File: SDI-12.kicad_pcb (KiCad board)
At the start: 2 copper layers, 61 x 30.3 mm, 44 parts, among them J1 USB_B_Micro, J2 Conn_SWD, J3 SDI-12_OUT, J4 SDI12_POWER, Q1 BSS138, Q2 BSS138, Q3 BSS138, U1 LDI1117-3.3H, U2 STM32F103C8Tx, U3 74LVC1G125GW,125, Y1 24MHz 15pF

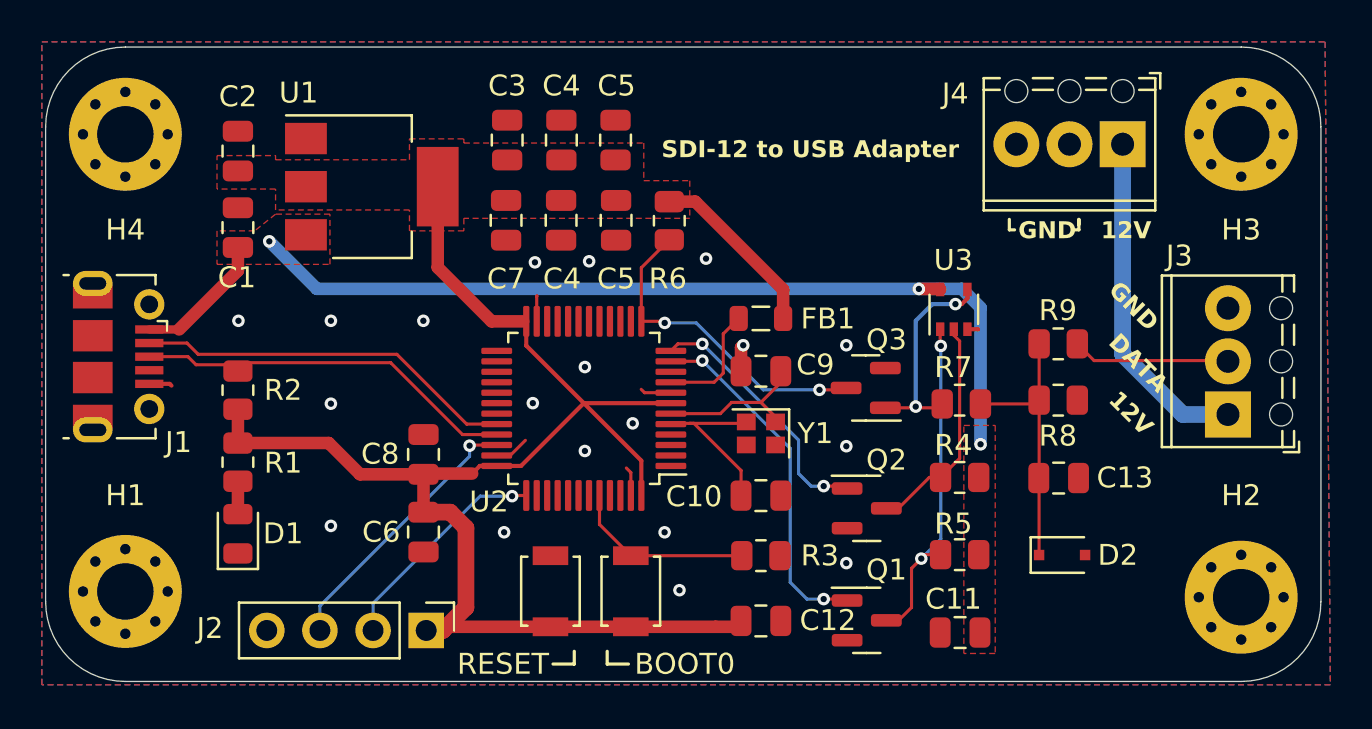
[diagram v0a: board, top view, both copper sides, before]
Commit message: - Crystal oscillator value changed to proper 16MHz - Minor font changes - Readme document - git lfs for readme graphics
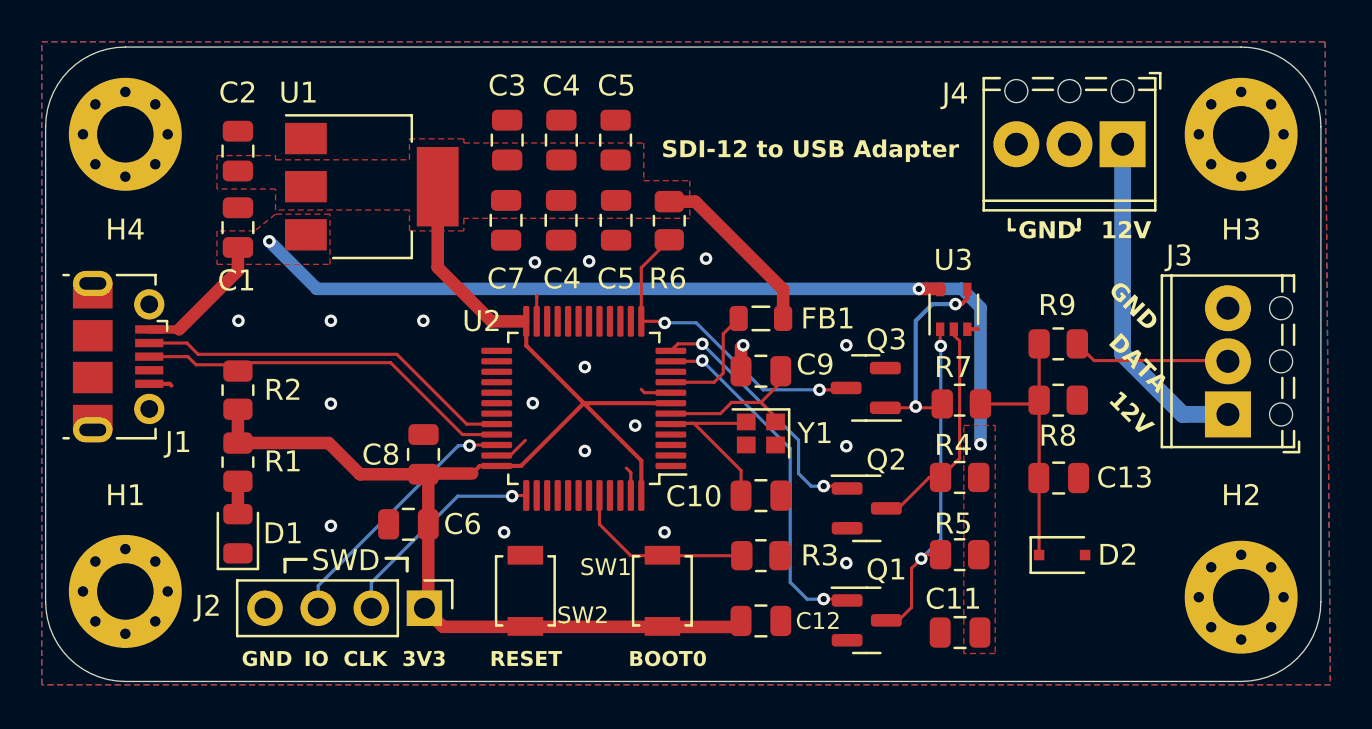
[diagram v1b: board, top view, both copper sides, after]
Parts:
- removed BOOT0: SW_Push, Button_Switch_SMD:SW_SPST_B3U-1000P
- removed RESET: RESET_SW, Button_Switch_SMD:SW_SPST_B3U-1000P
- added SW1: SW_Push, Button_Switch_SMD:SW_SPST_B3U-1000P, F.Cu at (66.5, 42.8)
- added SW2: RESET_SW, Button_Switch_SMD:SW_SPST_B3U-1000P, F.Cu at (59.9, 42.8)
- C10, C9: value 24pF -> 12pF
- Y1: value 24MHz 15pF -> 16MHz
- moved J2 1.06 mm to (55.1, 43.6)
- moved C6 0.81 mm to (54.3, 39.6), turned to 0 degrees
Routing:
- net 3V3: track 77.8 -> 75.2 mm
- net SWDIO: track 13.1 -> 12.4 mm
- net GND: vias 19 -> 18
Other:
- board text added: "3V3"
- board text added: "BOOT0"
- board text added: "CLK"
- board text added: "IO"
- board text added: "RESET"
- board text added: "SWD"

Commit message: - STM32F103 replaced with G431 counterpart - TXS0102x for voltage level shifting - Added LED's for I/O status
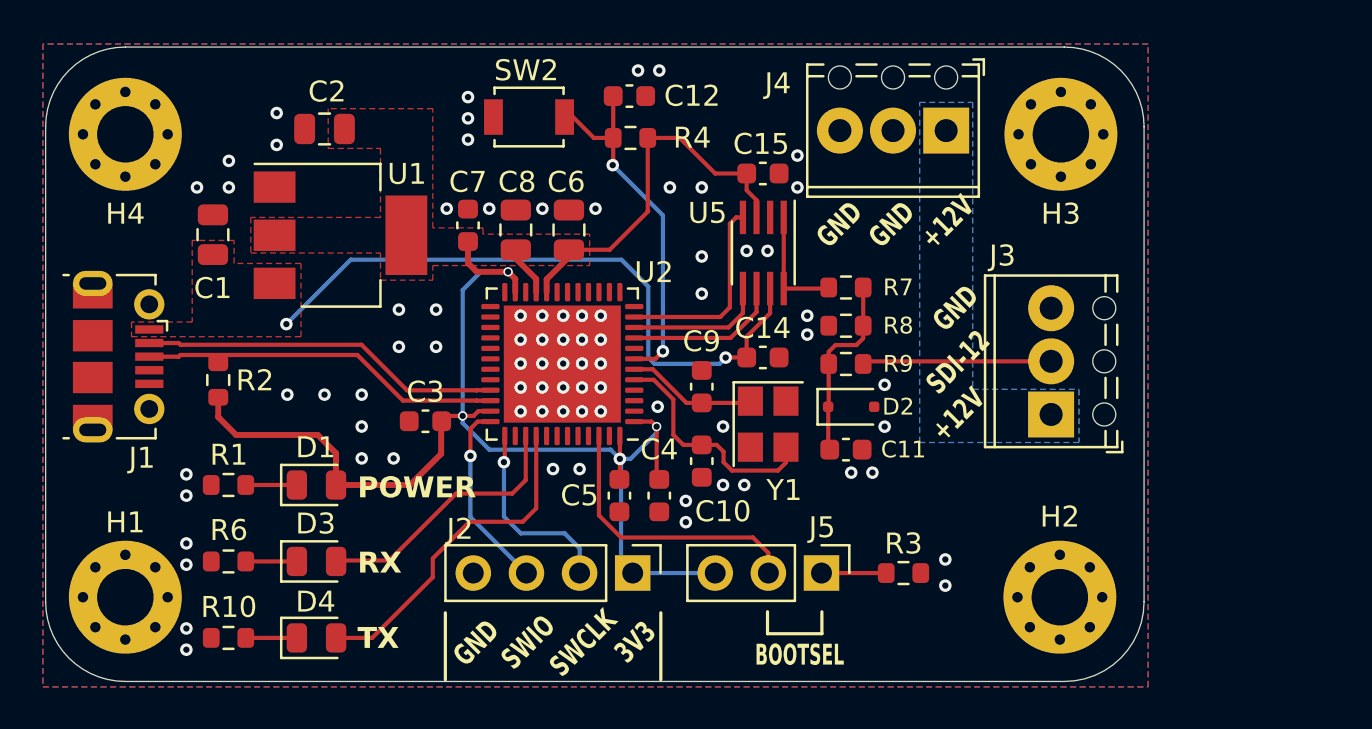
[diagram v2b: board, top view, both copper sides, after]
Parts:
- removed C13: 22nF, Capacitor_SMD:C_0805_2012Metric
- removed the C4 at (61.6, 21.2)
- removed the C4 at (61.6, 25.0)
- removed the C5 at (64.2, 21.2)
- removed the C5 at (64.3, 25.0)
- removed FB1: 100MHz 1kΩ, Inductor_SMD:L_0805_2012Metric
- removed Q1, Q2, Q3: BSS138, Package_TO_SOT_SMD:SOT-23
- removed R5: 2.2kΩ, Resistor_SMD:R_0805_2012Metric
- removed SW1: SW_Push, Button_Switch_SMD:SW_SPST_B3U-1000P
- removed U3: 74LVC1G125GW,125, Package_TO_SOT_SMD:SOT-353_SC-70-5
- added C14: 100nF, Capacitor_SMD:C_0603_1608Metric, F.Cu at (71.3, 31.6)
- added C15: 100nF, Capacitor_SMD:C_0603_1608Metric, F.Cu at (71.3, 22.8)
- added C4: 100nF, Capacitor_SMD:C_0603_1608Metric, F.Cu at (66.3, 38.2)
- added C5: 100nF, Capacitor_SMD:C_0603_1608Metric, F.Cu at (64.4, 38.2)
- added D3: USER_LED, LED_SMD:LED_0805_2012Metric, F.Cu at (49.9, 41.3)
- added D4: USER_LED_2, LED_SMD:LED_0805_2012Metric, F.Cu at (49.9, 45.0)
- added J5: BOOTSEL, Connector_PinHeader_2.54mm:PinHeader_1x03_P2.54mm_Vertical, F.Cu at (74.1, 41.9)
- added R10: xkΩ, Resistor_SMD:R_0603_1608Metric, F.Cu at (45.7, 45.0)
- added U5: TXS0102DCT, Package_SO:SSOP-8_2.95x2.8mm_P0.65mm, F.Cu at (71.3, 26.6)
- C10, C12, C3, C7, C9: footprint Capacitor_SMD:C_0805_2012Metric -> Capacitor_SMD:C_0603_1608Metric
- C11: value 100nF -> 22nF; footprint Capacitor_SMD:C_0805_2012Metric -> Capacitor_SMD:C_0603_1608Metric
- D1: value G_LED -> RED_LED
- R1: value 1kΩ -> xkΩ; footprint Resistor_SMD:R_0805_2012Metric -> Resistor_SMD:R_0603_1608Metric
- R2, R3, R7, R8, R9: footprint Resistor_SMD:R_0805_2012Metric -> Resistor_SMD:R_0603_1608Metric
- R4: value 2.2kΩ -> DNP; footprint Resistor_SMD:R_0805_2012Metric -> Resistor_SMD:R_0603_1608Metric
- R6: value 2.2kΩ -> xkΩ; footprint Resistor_SMD:R_0805_2012Metric -> Resistor_SMD:R_0603_1608Metric
- SW2: value RESET_SW -> RESET
- U2: value STM32F103C8Tx -> STM32G431CBUx; footprint Package_QFP:LQFP-48_7x7mm_P0.5mm -> Package_DFN_QFN:QFN-48-1EP_7x7mm_P0.5mm_EP5.6x5.6mm
- Y1: value 16MHz -> 24MHz; footprint Crystal:Crystal_SMD_2016-4Pin_2.0x1.6mm -> Crystal:Crystal_SMD_3225-4Pin_3.2x2.5mm
- moved R6 26.6 mm to (45.7, 41.3), turned to 0 degrees
- moved C12 25.9 mm to (64.9, 19.1)
- moved SW2 22.7 mm to (60.1, 20.1), turned to 180 degrees
- moved R4 22.6 mm to (65.0, 21.1)
- moved C6 16.0 mm to (62.0, 25.5), turned to -90 degrees
- moved C3 14.0 mm to (55.1, 34.6), turned to 0 degrees
- moved D2 12.3 mm to (75.5, 34.0)
- moved C8 11.6 mm to (59.5, 25.5)
- moved R8 10.8 mm to (75.2, 30.1), turned to 180 degrees
- moved C11 10.3 mm to (75.2, 36.0), turned to 0 degrees
- moved R9 10.2 mm to (75.2, 31.9)
- moved J2 10.1 mm to (65.1, 41.9)
- moved H2 8.67 mm to (85.5, 43.1)
- moved H3 8.62 mm to (85.5, 20.9)
- moved J4 8.46 mm to (80.0, 20.8)
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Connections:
- net SDI-12_DATA renamed SDI-12_BUS
- C11 pad 1: 5V -> Net-(D2-K)
- C12 pad 1: 3V3 -> NRST
- D1 pad 1: GND -> Net-(D1-K)
- D1 pad 2: Net-(D1-A) -> 3V3
- R1 pad 1: Net-(D1-A) -> GND
- R1 pad 2: 3V3 -> Net-(D1-K)
- R3 pad 1: BOOT0 -> Net-(J5-Pin_1)
- R4 pad 1: 5V -> 3V3
- R4 pad 2: Net-(Q2-D) -> NRST
- R6 pad 1: 3V3 -> GND
- R6 pad 2: SDI-12_RX -> Net-(D3-K)
- R7 pad 2: Net-(Q3-G) -> SDI-12_CIRCUIT
- SW2 pad 1: 3V3 -> NRST
- U2 pad 1: VBAT -> 3V3
- U2 pad 10: unconnected-(U2-PA0-Pad10) -> SDI-12_MCU
- U2 pad 11: SDI-12_EN -> SDI-12_MCU_AUX
- U2 pad 12: SDI-12_TX -> unconnected-(U2-PA4-Pad12)
- U2 pad 13: SDI-12_RX -> unconnected-(U2-PA5-Pad13)
- U2 pad 20: unconnected-(U2-PB2-Pad20) -> 3V3
- U2 pad 21: unconnected-(U2-PB10-Pad21) -> 3V3
- U2 pad 23: GND -> 3V3
- U2 pad 24: 3V3 -> unconnected-(U2-PB11-Pad24)
- U2 pad 32: USB_D- -> unconnected-(U2-PA10-Pad32)
- U2 pad 33: USB_D+ -> USB_D-
- U2 pad 34: SWDIO -> USB_D+
- U2 pad 35: GND -> 3V3
- U2 pad 36: 3V3 -> SWDIO
- U2 pad 39: unconnected-(U2-PB3-Pad39) -> USER_LED_1
- U2 pad 40: unconnected-(U2-PB4-Pad40) -> USER_LED_2
- U2 pad 44: BOOT0 -> unconnected-(U2-PB6-Pad44)
- U2 pad 46: unconnected-(U2-PB9-Pad46) -> BOOT0
- U2 pad 47: GND -> unconnected-(U2-PB9-Pad47)
- U2 pad 7: 3V3 -> NRST
- U2 pad 8: GND -> unconnected-(U2-PA0-Pad8)
- U2 pad 9: Net-(U2-VDDA) -> SDI-12_EN
- Y1 pad 2: HSE_OSC_IN -> GND
- Y1 pad 3: (no net) -> HSE_OSC_IN
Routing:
- net 5V: track 49.5 -> 31.2 mm, vias 3 -> 2
- net NRST: track 0.00 -> 17.5 mm, vias 0 -> 2
- net Net-(Q1-D): track 16.4 -> 0.00 mm, vias 2 -> 0
- net 12V: track 16.3 -> 0.00 mm
- net USER_LED_2: track 0.00 -> 16.1 mm
- net SDI-12_RX: track 15.6 -> 0.00 mm, vias 2 -> 0
- net USER_LED_1: track 0.00 -> 12.7 mm
- net SDI-12_TX: track 12.4 -> 0.00 mm, vias 2 -> 0
- net Net-(Q2-D): track 10.8 -> 0.00 mm
- net Net-(Q3-G): track 10.2 -> 0.00 mm, vias 2 -> 0
- net SDI-12_MCU_AUX: track 0.00 -> 9.51 mm
- net SDI-12_EN: track 16.9 -> 7.48 mm, vias 2 -> 0
- net GND: track 8.68 -> 0.00 mm, vias 18 -> 79
- net SDI-12_MCU: track 0.00 -> 6.65 mm
- net Net-(U2-VDDA): track 5.60 -> 0.00 mm
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- added copper zone on B.Cu, net 12V
- added copper zone on In1.Cu, net GND
- added copper zone on In2.Cu, net GND
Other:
- board size 61 x 30.3 mm -> 52.5 x 30.3 mm
- copper layers 2 -> 4
- board text added: "+12V"
- board text added: "BOOTSEL"
- board text added: "POWER"
- board text added: "RX"
- board text added: "SDI-12"
- board text added: "SWCLK"
- board text added: "SWIO"
- board text added: "TX"
- board text removed: "12V"
- board text removed: "BOOT0"
- board text removed: "CLK"
- board text removed: "DATA"
- board text removed: "IO"
- board text removed: "JLCJLCJLCJLC"
- board text removed: "RESET"
- board text removed: "SDI-12 to USB Adapter"
- board text removed: "SWD"
